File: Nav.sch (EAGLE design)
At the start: 47 parts, among them J1 U.FL-R-SMT, SW5 THAU13-AB-R, SW6 THAU13-AB-R, SW7 TVAF06-A020B-R, SW8 TVAF06-A020B-R, U1 LSM9DS1, U2 LPS25HB, U6 OPA340N, U7 DRIVER-LV8548MC-AH(SOIC10), U8 I-02247_NJM2845

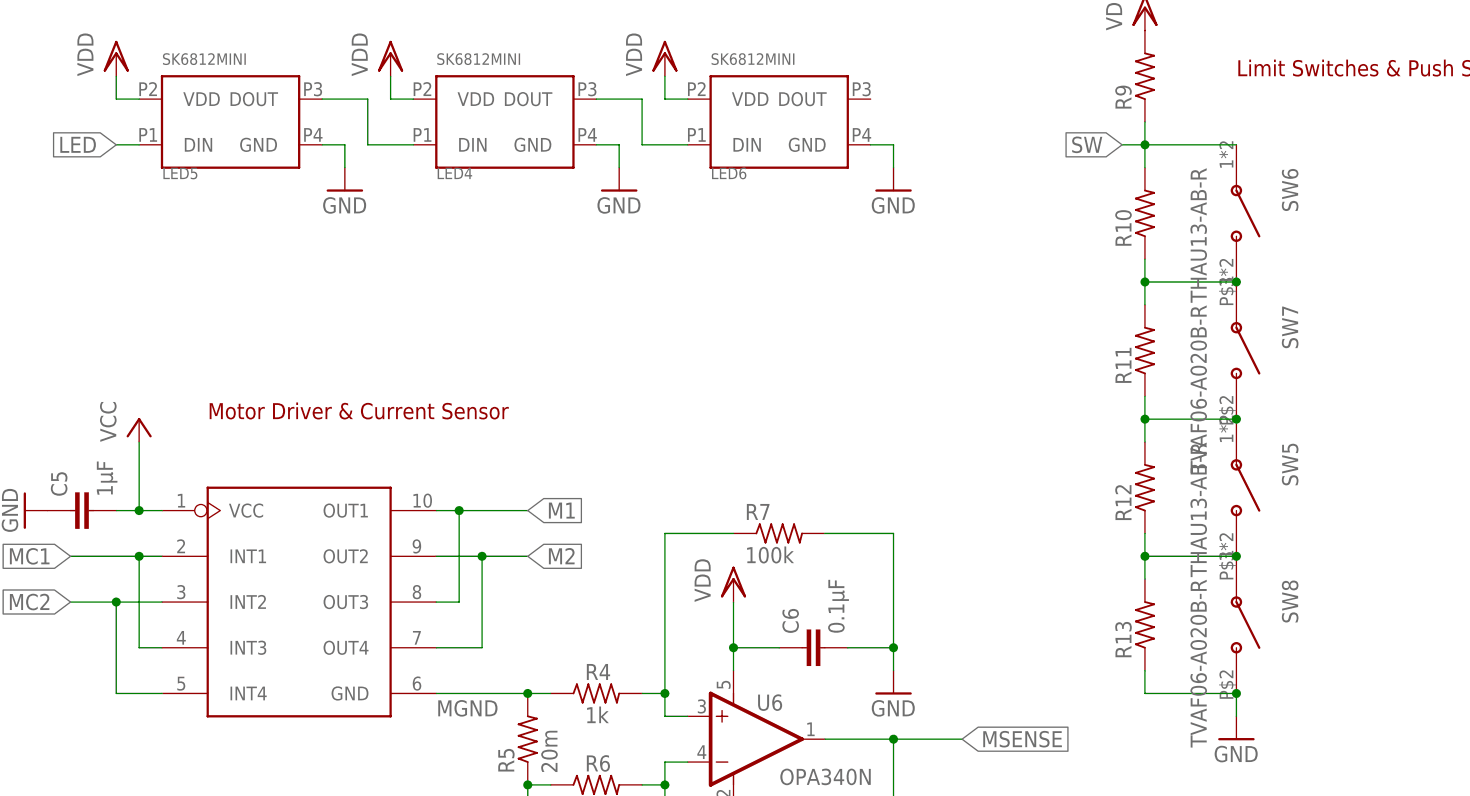
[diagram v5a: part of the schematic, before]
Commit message: Format silk
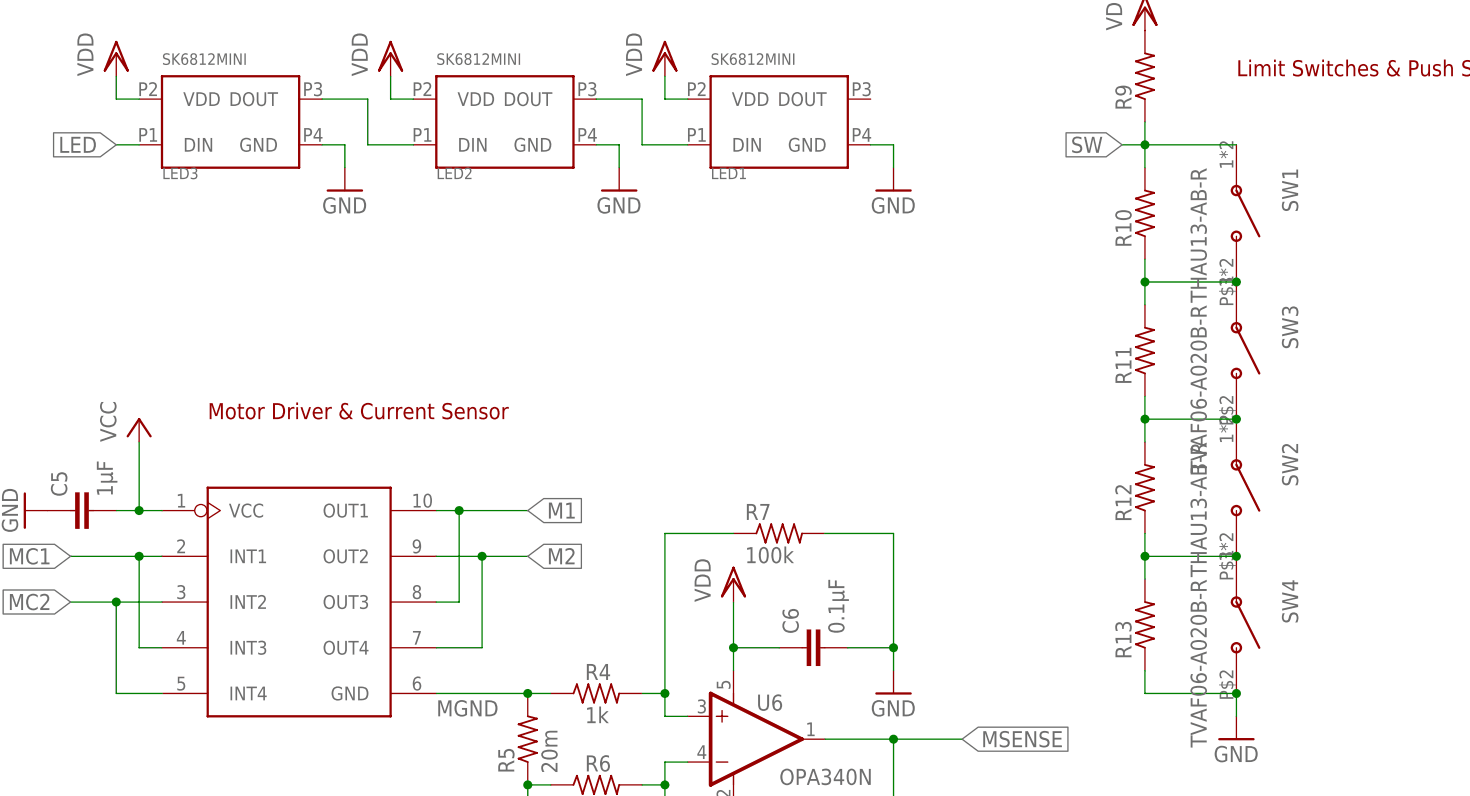
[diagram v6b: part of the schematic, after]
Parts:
- renumbered LED4 to LED2, LED5 to LED3, LED6 to LED1, SW5 to SW2, SW6 to SW1, SW7 to SW3, SW8 to SW4
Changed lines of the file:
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@@
 <part name="GND45" library="supply1" library_urn="urn:adsk.eagle:library:371" deviceset="GND" device=""/>
 <part name="R1" library="rcl" library_urn="urn:adsk.eagle:library:334" deviceset="R-US_" device="R0603" package3d_urn="urn:adsk.eagle:package:23555/3" value="100k"/>
-<part name="SW5" library="switches" deviceset="THAU13-AB-R" device=""/>
-<part name="SW6" library="switches" deviceset="THAU13-AB-R" device=""/>
+<part name="SW2" library="switches" deviceset="THAU13-AB-R" device=""/>
+<part name="SW1" library="switches" deviceset="THAU13-AB-R" device=""/>
 <part name="C4" library="rcl" library_urn="urn:adsk.eagle:library:334" deviceset="C-EU" device="C0603" package3d_urn="urn:adsk.eagle:package:23616/2" value="0.1µF"/>
 <part name="GND46" library="supply1" library_urn="urn:adsk.eagle:library:371" deviceset="GND" device=""/>
-<part name="LED4" library="leds" deviceset="SK6812MINI" device=""/>
-<part name="LED5" library="leds" deviceset="SK6812MINI" device=""/>
+<part name="LED2" library="leds" deviceset="SK6812MINI" device=""/>
+<part name="LED3" library="leds" deviceset="SK6812MINI" device=""/>
 <part name="VDD19" library="supply1" library_urn="urn:adsk.eagle:library:371" deviceset="VDD" device=""/>
 <part name="VDD20" library="supply1" library_urn="urn:adsk.eagle:library:371" deviceset="VDD" device=""/>
 <part name="GND47" library="supply1" library_urn="urn:adsk.eagle:library:371" deviceset="GND" device=""/>
 <part name="GND48" library="supply1" library_urn="urn:adsk.eagle:library:371" deviceset="GND" device=""/>
-<part name="SW7" library="switches" deviceset="TVAF06-A020B-R" device=""/>
-<part name="LED6" library="leds" deviceset="SK6812MINI" device=""/>
+<part name="SW3" library="switches" deviceset="TVAF06-A020B-R" device=""/>
+<part name="LED1" library="leds" deviceset="SK6812MINI" device=""/>
 <part name="GND49" library="supply1" library_urn="urn:adsk.eagle:library:371" deviceset="GND" device=""/>
 <part name="VDD21" library="supply1" library_urn="urn:adsk.eagle:library:371" deviceset="VDD" device=""/>
@@
 <part name="VDD22" library="supply1" library_urn="urn:adsk.eagle:library:371" deviceset="VDD" device=""/>
 <part name="GND50" library="supply1" library_urn="urn:adsk.eagle:library:371" deviceset="GND" device=""/>
-<part name="SW8" library="switches" deviceset="TVAF06-A020B-R" device=""/>
+<part name="SW4" library="switches" deviceset="TVAF06-A020B-R" device=""/>
 </parts>
 <sheets>
@@
 <attribute name="VALUE" x="80.01" y="145.542" size="1.778" layer="96" rot="R180"/>
 </instance>
-<instance part="SW5" gate="G$1" x="264.16" y="104.14" smashed="yes" rot="R270">
+<instance part="SW2" gate="G$1" x="264.16" y="104.14" smashed="yes" rot="R270">
 <attribute name="NAME" x="269.24" y="109.22" size="1.778" layer="95" rot="R270"/>
 <attribute name="VALUE" x="259.08" y="109.22" size="1.778" layer="96" rot="R270"/>
 </instance>
-<instance part="SW6" gate="G$1" x="264.16" y="134.62" smashed="yes" rot="R270">
+<instance part="SW1" gate="G$1" x="264.16" y="134.62" smashed="yes" rot="R270">
 <attribute name="NAME" x="269.24" y="139.7" size="1.778" layer="95" rot="R270"/>
 <attribute name="VALUE" x="259.08" y="139.7" size="1.778" layer="96" rot="R270"/>
@@
 <attribute name="VALUE" x="-5.08" y="45.72" size="1.778" layer="96"/>
 </instance>
-<instance part="LED4" gate="G$1" x="182.88" y="144.78" smashed="yes" rot="MR180">
+<instance part="LED2" gate="G$1" x="182.88" y="144.78" smashed="yes" rot="MR180">
 <attribute name="NAME" x="175.26" y="139.7" size="1.27" layer="95" rot="MR180"/>
 <attribute name="VALUE" x="175.26" y="152.4" size="1.27" layer="96" rot="MR180"/>
 </instance>
-<instance part="LED5" gate="G$1" x="152.4" y="144.78" smashed="yes" rot="MR180">
+<instance part="LED3" gate="G$1" x="152.4" y="144.78" smashed="yes" rot="MR180">
 <attribute name="NAME" x="144.78" y="139.7" size="1.27" layer="95" rot="MR180"/>
 <attribute name="VALUE" x="144.78" y="152.4" size="1.27" layer="96" rot="MR180"/>
@@
 <attribute name="VALUE" x="193.04" y="134.62" size="1.778" layer="96"/>
 </instance>
-<instance part="SW7" gate="G$1" x="264.16" y="119.38" smashed="yes" rot="R270">
+<instance part="SW3" gate="G$1" x="264.16" y="119.38" smashed="yes" rot="R270">
 <attribute name="NAME" x="269.24" y="124.46" size="1.778" layer="95" rot="R270"/>
 <attribute name="VALUE" x="259.08" y="124.46" size="1.778" layer="96" rot="R270"/>
 </instance>
-<instance part="LED6" gate="G$1" x="213.36" y="144.78" smashed="yes" rot="MR180">
+<instance part="LED1" gate="G$1" x="213.36" y="144.78" smashed="yes" rot="MR180">
 <attribute name="NAME" x="205.74" y="139.7" size="1.27" layer="95" rot="MR180"/>
 <attribute name="VALUE" x="205.74" y="152.4" size="1.27" layer="96" rot="MR180"/>
@@
 <attribute name="VALUE" x="261.62" y="73.66" size="1.778" layer="96"/>
 </instance>
-<instance part="SW8" gate="G$1" x="264.16" y="88.9" smashed="yes" rot="R270">
+<instance part="SW4" gate="G$1" x="264.16" y="88.9" smashed="yes" rot="R270">
 <attribute name="NAME" x="269.24" y="93.98" size="1.778" layer="95" rot="R270"/>
 <attribute name="VALUE" x="259.08" y="93.98" size="1.778" layer="96" rot="R270"/>
@@
 </segment>
 <segment>
-<pinref part="LED5" gate="G$1" pin="GND"/>
+<pinref part="LED3" gate="G$1" pin="GND"/>
 <wire x1="162.56" y1="142.24" x2="165.1" y2="142.24" width="0.1524" layer="91"/>
 <wire x1="165.1" y1="142.24" x2="165.1" y2="139.7" width="0.1524" layer="91"/>
@@
 </segment>
 <segment>
-<pinref part="LED4" gate="G$1" pin="GND"/>
+<pinref part="LED2" gate="G$1" pin="GND"/>
 <wire x1="193.04" y1="142.24" x2="195.58" y2="142.24" width="0.1524" layer="91"/>
 <wire x1="195.58" y1="142.24" x2="195.58" y2="139.7" width="0.1524" layer="91"/>
@@
 <wire x1="226.06" y1="142.24" x2="226.06" y2="139.7" width="0.1524" layer="91"/>
 <pinref part="GND49" gate="1" pin="GND"/>
-<pinref part="LED6" gate="G$1" pin="GND"/>
+<pinref part="LED1" gate="G$1" pin="GND"/>
 <wire x1="223.52" y1="142.24" x2="226.06" y2="142.24" width="0.1524" layer="91"/>
 </segment>
@@
 <wire x1="264.16" y1="81.28" x2="264.16" y2="78.74" width="0.1524" layer="91"/>
 <wire x1="254" y1="81.28" x2="264.16" y2="81.28" width="0.1524" layer="91"/>
-<pinref part="SW8" gate="G$1" pin="B"/>
+<pinref part="SW4" gate="G$1" pin="B"/>
 <junction x="264.16" y="81.28"/>
 <pinref part="R13" gate="G$1" pin="1"/>
@@
 </segment>
 <segment>
-<pinref part="LED4" gate="G$1" pin="VDD"/>
+<pinref part="LED2" gate="G$1" pin="VDD"/>
 <wire x1="172.72" y1="147.32" x2="170.18" y2="147.32" width="0.1524" layer="91"/>
 <wire x1="170.18" y1="147.32" x2="170.18" y2="149.86" width="0.1524" layer="91"/>
@@
 </segment>
 <segment>
-<pinref part="LED5" gate="G$1" pin="VDD"/>
+<pinref part="LED3" gate="G$1" pin="VDD"/>
 <wire x1="142.24" y1="147.32" x2="139.7" y2="147.32" width="0.1524" layer="91"/>
 <wire x1="139.7" y1="147.32" x2="139.7" y2="149.86" width="0.1524" layer="91"/>
@@
 <wire x1="200.66" y1="147.32" x2="200.66" y2="149.86" width="0.1524" layer="91"/>
 <pinref part="VDD21" gate="G$1" pin="VDD"/>
-<pinref part="LED6" gate="G$1" pin="VDD"/>
+<pinref part="LED1" gate="G$1" pin="VDD"/>
 <wire x1="200.66" y1="147.32" x2="203.2" y2="147.32" width="0.1524" layer="91"/>
 </segment>
@@
 <net name="N$17" class="0">
 <segment>
-<pinref part="LED5" gate="G$1" pin="DOUT"/>
+<pinref part="LED3" gate="G$1" pin="DOUT"/>
 <wire x1="162.56" y1="147.32" x2="167.64" y2="147.32" width="0.1524" layer="91"/>
 <wire x1="167.64" y1="147.32" x2="167.64" y2="142.24" width="0.1524" layer="91"/>
-<pinref part="LED4" gate="G$1" pin="DIN"/>
+<pinref part="LED2" gate="G$1" pin="DIN"/>
 <wire x1="167.64" y1="142.24" x2="172.72" y2="142.24" width="0.1524" layer="91"/>
 </segment>
@@
 <net name="LED" class="0">
 <segment>
-<pinref part="LED5" gate="G$1" pin="DIN"/>
+<pinref part="LED3" gate="G$1" pin="DIN"/>
 <wire x1="142.24" y1="142.24" x2="139.7" y2="142.24" width="0.1524" layer="91"/>
 <label x="139.7" y="142.24" size="1.778" layer="95" rot="R180" xref="yes"/>
@@
 <net name="N$18" class="0">
 <segment>
-<pinref part="LED4" gate="G$1" pin="DOUT"/>
+<pinref part="LED2" gate="G$1" pin="DOUT"/>
 <wire x1="193.04" y1="147.32" x2="198.12" y2="147.32" width="0.1524" layer="91"/>
 <wire x1="198.12" y1="147.32" x2="198.12" y2="142.24" width="0.1524" layer="91"/>
-<pinref part="LED6" gate="G$1" pin="DIN"/>
+<pinref part="LED1" gate="G$1" pin="DIN"/>
 <wire x1="203.2" y1="142.24" x2="198.12" y2="142.24" width="0.1524" layer="91"/>
 </segment>
@@
 <pinref part="R10" gate="G$1" pin="2"/>
 <wire x1="254" y1="144.78" x2="254" y2="142.24" width="0.1524" layer="91"/>
-<pinref part="SW6" gate="G$1" pin="A"/>
+<pinref part="SW1" gate="G$1" pin="A"/>
 <wire x1="254" y1="142.24" x2="254" y2="139.7" width="0.1524" layer="91"/>
 <wire x1="254" y1="142.24" x2="264.16" y2="142.24" width="0.1524" layer="91"/>
@@
 <pinref part="R11" gate="G$1" pin="1"/>
 <wire x1="254" y1="114.3" x2="254" y2="111.76" width="0.1524" layer="91"/>
-<pinref part="SW7" gate="G$1" pin="B"/>
-<pinref part="SW5" gate="G$1" pin="A"/>
+<pinref part="SW3" gate="G$1" pin="B"/>
+<pinref part="SW2" gate="G$1" pin="A"/>
 <wire x1="254" y1="111.76" x2="254" y2="109.22" width="0.1524" layer="91"/>
 <wire x1="254" y1="111.76" x2="264.16" y2="111.76" width="0.1524" layer="91"/>
@@
 <net name="N$20" class="0">
 <segment>
-<pinref part="SW6" gate="G$1" pin="B"/>
-<pinref part="SW7" gate="G$1" pin="A"/>
+<pinref part="SW1" gate="G$1" pin="B"/>
+<pinref part="SW3" gate="G$1" pin="A"/>
 <wire x1="264.16" y1="127" x2="254" y2="127" width="0.1524" layer="91"/>
 <junction x="264.16" y="127"/>
@@
 <pinref part="R12" gate="G$1" pin="1"/>
 <wire x1="254" y1="99.06" x2="254" y2="96.52" width="0.1524" layer="91"/>
-<pinref part="SW5" gate="G$1" pin="B"/>
+<pinref part="SW2" gate="G$1" pin="B"/>
 <wire x1="254" y1="96.52" x2="264.16" y2="96.52" width="0.1524" layer="91"/>
-<pinref part="SW8" gate="G$1" pin="A"/>
+<pinref part="SW4" gate="G$1" pin="A"/>
 <junction x="264.16" y="96.52"/>
 <pinref part="R13" gate="G$1" pin="2"/>
